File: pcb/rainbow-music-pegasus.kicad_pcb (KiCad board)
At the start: 2 copper layers, 151 x 31 mm, 114 parts, among them J1 USB_B_Micro, J2 Conn_02x03_Odd_Even, J3 B2B-PH-K-S, Q1 DMG3415U, SW1 SW_SPDT, SW2 EVQQ2, U1 ESP32-C3-MINI-1, U2 OPA2322, U3 TLV75533PDBV, U4 MCP73831-2-OT, U5 MCP41050

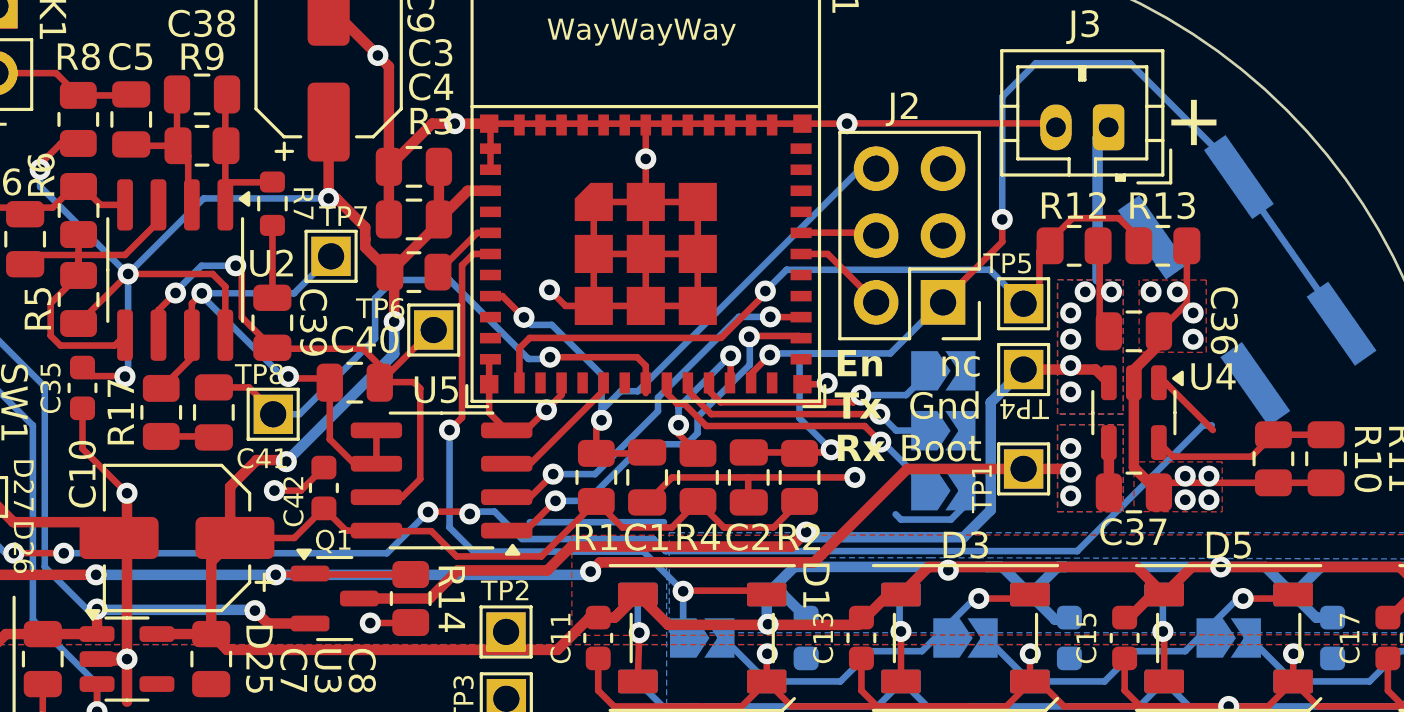
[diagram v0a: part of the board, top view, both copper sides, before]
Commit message: Minor changes to the PCB and BOM to better support the digipot and signal
* Remove C40 (which was shunting the MCP41050 PB0 & PB0, reducing effectiveness)
* Raise R7 from 470 to 2.2k
* Raise R17 from 100 to 330
* Change C41 to a 0.1uF shunt cap to GND placed close to GPIO4

The R7 is raised 2.2k so the digipot wiper current stays within its +/-1
mA rating even if the first stage swings rail to rail, and so loud music
sits mid-range on the wiper where steps are finer (maximum stage-2 gain
is now ~23). With C39 (2.2uF) this also lowers the high-pass corner from
~154 Hz to ~33 Hz, letting bass through.

The ADC now sees U2B's 1.65 V output directly, as the firmware expects,
and R17/C41 form a ~4.8 kHz anti-aliasing filter and a charge reservoir
for ADC sampling.
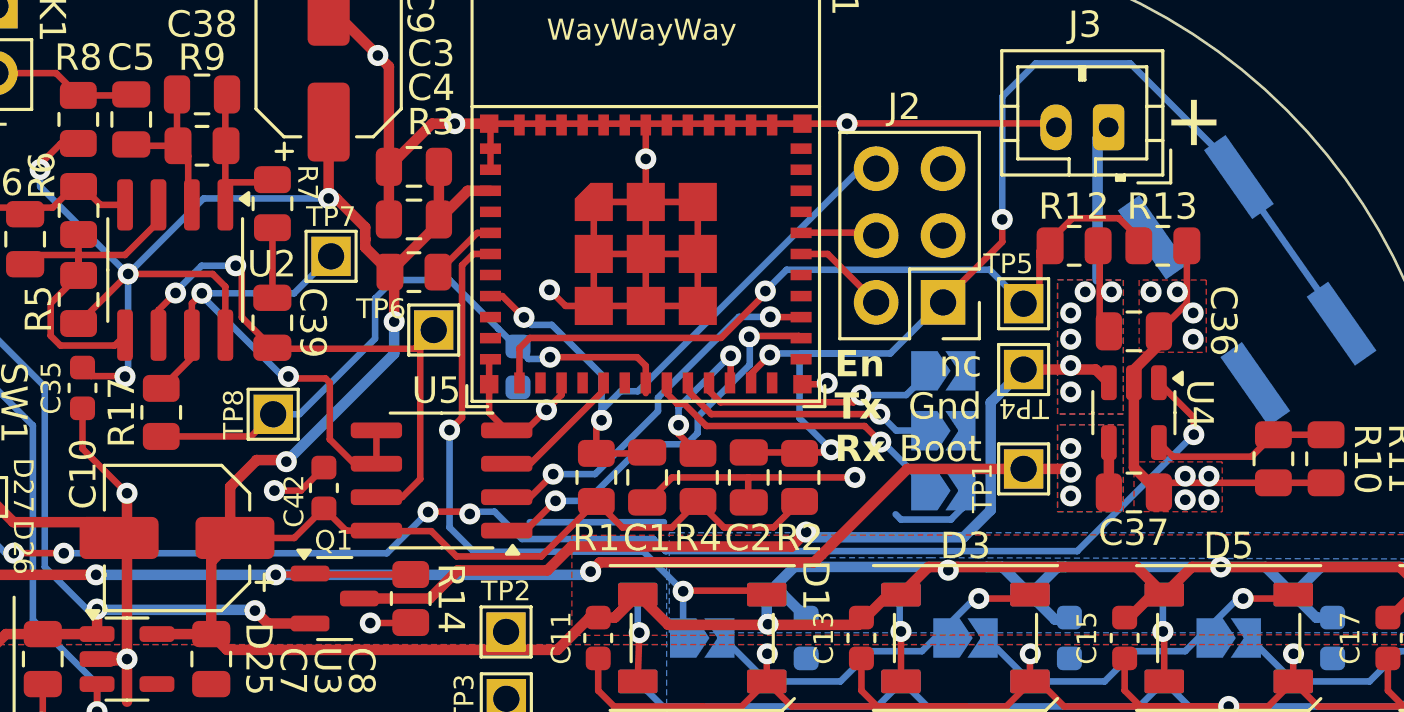
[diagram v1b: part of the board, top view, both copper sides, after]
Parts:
- removed C40: 4.7uF, Capacitor_SMD:C_0805_2012Metric
- C41: value 2.2uF -> 0.1uF; footprint Capacitor_SMD:C_0805_2012Metric -> Capacitor_SMD:C_0603_1608Metric; moved to B.Cu
- R17: value 100 -> 330
- R7: value 470 -> 2.2k; footprint Resistor_SMD:R_0603_1608Metric -> Resistor_SMD:R_0805_2012Metric
- moved C41 11.7 mm to (108.8, 90.3)
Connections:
- C41 pad 2: Net-(C41-Pad2) -> GND
- R17 pad 2: Net-(C41-Pad2) -> /Mic_Signal
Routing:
- net Net-(C41-Pad2): track 2.02 -> 0.00 mm
- net /Mic_Signal: track 22.4 -> 24.3 mm
- net Net-(U4-STAT): track 54.4 -> 53.3 mm, vias 4 -> 5
- net /DP_B: track 23.2 -> 22.6 mm
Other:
- board text added: "v1.1.1"
- board text removed: "v1.1"

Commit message: Move the button from GPIO9 to GPIO1
Eventually the button will be used as a factory reset (remove settings
like wifi configuration, etc) by holding down on power-on.  You cannot
do that with GPIO9 as that is already used to launch the bootloader on
power-on.

Actual button code and functionality still TBD.
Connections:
- C2 pad 2: /Boot -> /Button
- R2 pad 2: /Boot -> /Button
- SW2 pad 1: /Boot -> /Button
- U1 pad 13: unconnected-(U1-GPIO1/ADC1_CH1/XTAL_32K_N-Pad13) -> /Button
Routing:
- net /Button: track 0.00 -> 53.6 mm, vias 0 -> 3
- net /Boot: track 46.1 -> 11.8 mm, vias 3 -> 1
- net GND: track 458.8 -> 461.7 mm

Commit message: Change C38 to a 1.5nF C0G
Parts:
- C38: value 100pF -> 1.5nF C0G
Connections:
- C38 pad 1: Net-(U2A--) -> Net-(C38-Pad1)
- C38 pad 2: Net-(C38-Pad2) -> Net-(U2A--)
- R7 pad 1: Net-(C38-Pad2) -> Net-(C38-Pad1)
- R9 pad 1: Net-(C38-Pad2) -> Net-(U2A--)
- R9 pad 2: Net-(U2A--) -> Net-(C38-Pad1)
- U2 pad 1: Net-(C38-Pad2) -> Net-(C38-Pad1)
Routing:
- net Net-(U2A--): track 6.23 -> 13.0 mm
- net Net-(C38-Pad2): track 6.76 -> 0.00 mm
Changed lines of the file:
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@@
 			(layers "F.Cu" "F.Mask" "F.Paste")
 			(roundrect_rratio 0.243902)
-			(net "Net-(C38-Pad2)")
+			(net "Net-(C38-Pad1)")
 			(pintype "passive")
 		)
@@
 			)
 		)
-		(property "Value" "100pF"
+		(property "Value" "1.5nF C0G"
 			(at 0 1.68 0)
 			(layer "F.Fab")
@@
 			(layers "F.Cu" "F.Mask" "F.Paste")
 			(roundrect_rratio 0.25)
-			(net "Net-(U2A--)")
+			(net "Net-(C38-Pad1)")
 			(pintype "passive")
 		)
@@
 			(layers "F.Cu" "F.Mask" "F.Paste")
 			(roundrect_rratio 0.25)
-			(net "Net-(C38-Pad2)")
+			(net "Net-(U2A--)")
 			(pintype "passive")
 		)
@@
 			(layers "F.Cu" "F.Mask" "F.Paste")
 			(roundrect_rratio 0.25)
-			(net "Net-(C38-Pad2)")
+			(net "Net-(C38-Pad1)")
 			(pintype "output")
 		)
@@
 			(layers "F.Cu" "F.Mask" "F.Paste")
 			(roundrect_rratio 0.243902)
-			(net "Net-(C38-Pad2)")
+			(net "Net-(U2A--)")
 			(pintype "passive")
 		)
@@
 			(layers "F.Cu" "F.Mask" "F.Paste")
 			(roundrect_rratio 0.243902)
-			(net "Net-(U2A--)")
+			(net "Net-(C38-Pad1)")
 			(pintype "passive")
 		)
@@
 	)
 	(segment
-		(start 97.6825 84.145)
-		(end 97.6825 83.475)
+		(start 99.4725 87.67)
+		(end 99.4675 87.675)
 		(width 0.25)
 		(layer "F.Cu")
-		(net "Net-(C38-Pad2)")
+		(net "Net-(C39-Pad1)")
 	)
 	(segment
-		(start 97.6825 83.475)
-		(end 97.8675 83.29)
+		(start 99.4725 85.0125)
+		(end 99.4725 87.67)
 		(width 0.25)
 		(layer "F.Cu")
-		(net "Net-(C38-Pad2)")
+		(net "Net-(C39-Pad1)")
 	)
 	(segment
-		(start 99.4575 83.29)
-		(end 99.4725 83.275)
+		(start 97.6825 84.145)
+		(end 97.6825 83.475)
 		(width 0.25)
 		(layer "F.Cu")
-		(net "Net-(C38-Pad2)")
+		(net "Net-(U2A--)")
 	)
 	(segment
-		(start 97.8675 83.29)
-		(end 99.4575 83.29)
+		(start 97.6825 83.475)
+		(end 97.8675 83.29)
 		(width 0.25)
 		(layer "F.Cu")
-		(net "Net-(C38-Pad2)")
+		(net "Net-(U2A--)")
 	)
 	(segment
-		(start 97.6825 80.015)
-		(end 97.7475 79.95)
+		(start 94.1075 81.85)
+		(end 94.1575 81.9)
 		(width 0.25)
 		(layer "F.Cu")
-		(net "Net-(C38-Pad2)")
+		(net "Net-(U2A--)")
 	)
 	(segment
-		(start 97.6825 84.145)
-		(end 97.6825 80.015)
+		(start 96.2725 84.005)
+		(end 96.4125 84.145)
 		(width 0.25)
 		(layer "F.Cu")
-		(net "Net-(C38-Pad2)")
+		(net "Net-(U2A--)")
 	)
 	(segment
-		(start 99.4725 87.67)
-		(end 99.4675 87.675)
+		(start 94.1575 81.9)
+		(end 95.885 81.9)
 		(width 0.25)
 		(layer "F.Cu")
-		(net "Net-(C39-Pad1)")
+		(net "Net-(U2A--)")
 	)
 	(segment
-		(start 99.4725 85.0125)
-		(end 99.4725 87.67)
+		(start 95.8475 81.8625)
+		(end 95.885 81.9)
 		(width 0.25)
 		(layer "F.Cu")
-		(net "Net-(C39-Pad1)")
+		(net "Net-(U2A--)")
 	)
 	(segment
-		(start 94.1075 81.85)
-		(end 94.1575 81.9)
+		(start 99.4575 83.29)
+		(end 99.4725 83.275)
 		(width 0.25)
 		(layer "F.Cu")
@@
 	)
 	(segment
-		(start 96.2725 84.005)
-		(end 96.4125 84.145)
+		(start 95.885 81.9)
+		(end 96.2725 82.2875)
 		(width 0.25)
 		(layer "F.Cu")
@@
 	)
 	(segment
-		(start 94.1575 81.9)
-		(end 95.885 81.9)
+		(start 96.2725 82.2875)
+		(end 96.2725 84.005)
 		(width 0.25)
 		(layer "F.Cu")
@@
 	)
 	(segment
-		(start 95.8475 81.8625)
-		(end 95.885 81.9)
+		(start 97.8675 83.29)
+		(end 99.4575 83.29)
 		(width 0.25)
 		(layer "F.Cu")
@@
 	)
 	(segment
-		(start 95.885 81.9)
-		(end 96.2725 82.2875)
+		(start 97.6825 80.015)
+		(end 97.7475 79.95)
 		(width 0.25)
 		(layer "F.Cu")
@@
 	)
 	(segment
-		(start 96.2725 82.2875)
-		(end 96.2725 84.005)
+		(start 95.8475 79.95)
+		(end 95.8475 81.8625)
 		(width 0.25)
 		(layer "F.Cu")
@@
 	)
 	(segment
-		(start 95.8475 79.95)
-		(end 95.8475 81.8625)
+		(start 97.6825 84.145)
+		(end 97.6825 80.015)
 		(width 0.25)
 		(layer "F.Cu")

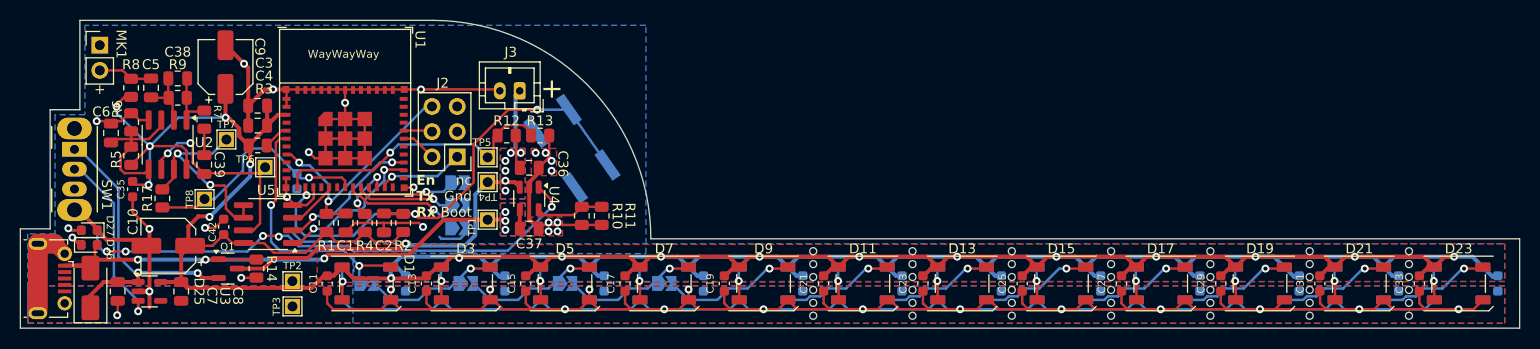
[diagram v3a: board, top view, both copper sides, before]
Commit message: Run DRC, adjust some cap placements
Cleaned up errors.  Still lots of warnings re: silkscreen violations
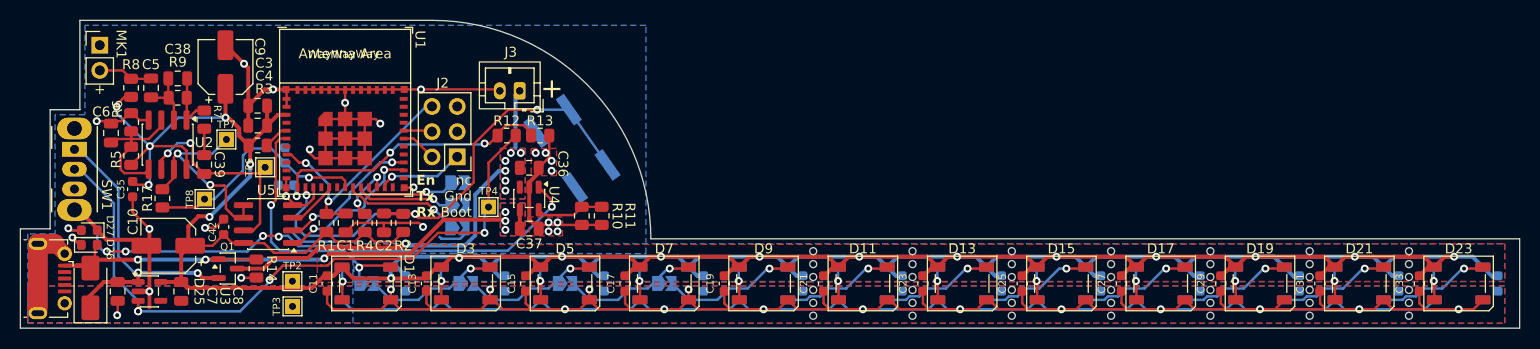
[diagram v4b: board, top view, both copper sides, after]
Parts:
- removed TP1, TP5: TestPoint, TestPoint:TestPoint_THTPad_1.5x1.5mm_Drill0.7mm
- added C40: 0.1uF, Capacitor_SMD:C_0603_1608Metric, B.Cu at (107.7, 90.7)
- moved C41 2.86 mm to (107.6, 87.7), turned to 90 degrees
- moved TP4 2.50 mm to (128.1, 92.9)
- turned C38 to 180 degrees
- turned R9 to 0 degrees
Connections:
- R12 pad 2: +BATT -> /SW_COM
- SW1 pad 2: Net-(SW1-B) -> /SW_COM
- TP4 pad 1: +BATT -> /SW_COM
- U3 pad 3: Net-(SW1-B) -> /SW_COM
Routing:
- net /SW_COM: track 0.00 -> 68.4 mm, vias 0 -> 4
- net Net-(SW1-B): track 18.3 -> 0.00 mm, vias 1 -> 0
- net Net-(C38-Pad1): track 0.00 -> 7.00 mm
- net Net-(U2A--): track 13.0 -> 6.43 mm
- net +BATT: track 44.2 -> 39.6 mm
- net GND: track 461.7 -> 463.7 mm, vias 36 -> 37
- net /Batt_Level: track 28.8 -> 30.2 mm, vias 1 -> 3

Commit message: Final cleanup of all DRC warnings — added to TODO to upgrade to USB-C
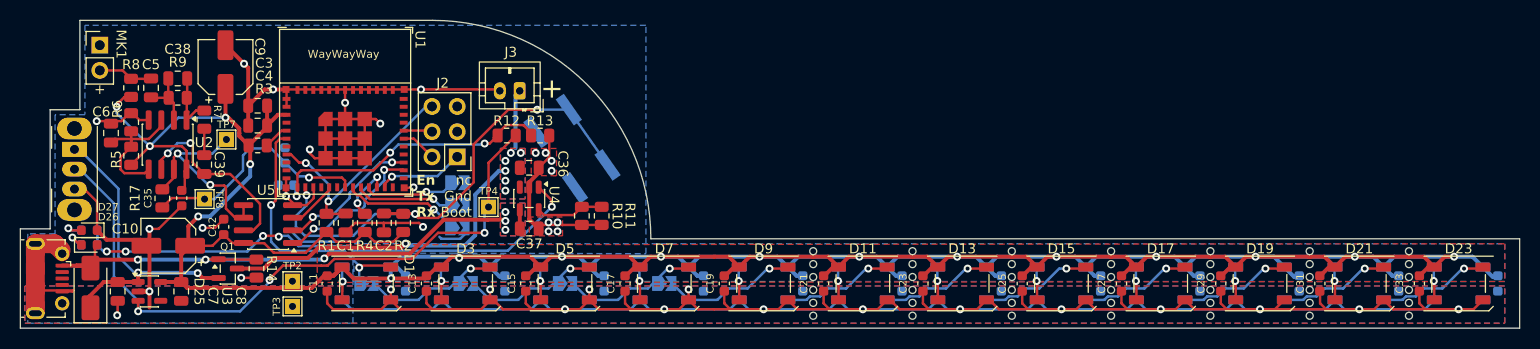
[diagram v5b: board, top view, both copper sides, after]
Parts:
- removed TP6: TestPoint, TestPoint:TestPoint_THTPad_1.5x1.5mm_Drill0.7mm
- SW1: footprint Button_Switch_THT:SW_CuK_OS102011MA1QN1_SPDT_Angled -> Button_Switch_THT:SW_Slide_SPDT_Angled_CK_OS102011MA1Q
- moved C35 5.02 mm to (97.2, 92.0)
- moved J1 0.25 mm to (83.7, 100.1)
- turned TP8 to 180 degrees
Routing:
- net GND: track 463.7 -> 471.6 mm
- net +3.3V: track 397.1 -> 393.6 mm, vias 18 -> 17
- net /DP_B: track 22.6 -> 19.2 mm
- net /SW_COM: vias 4 -> 3

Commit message: Replaced the dual 0603 power status LEDs with a LTST-C195KGJRKT
A little easier to place as the orientation is clear.
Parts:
- removed D27: GREEN, LED_SMD:LED_0603_1608Metric
- removed TP7: TestPoint, TestPoint:TestPoint_THTPad_1.5x1.5mm_Drill0.7mm
- C38: value 1.5nF C0G -> 6.8nF C0G
- D26: value RED -> LTST-C195KGJRKT; footprint LED_SMD:LED_0603_1608Metric -> Altivo:LTST-C195KGJRKT
- MK1: value Microphone -> AOM-5024P-HD-MB-R
- R9: value 10k -> 2.2k
- moved TP1 1.30 mm to (100.8, 92.1), turned to 0 degrees
- moved D26 0.73 mm to (87.7, 96.0), turned to 180 degrees
- moved C6 0.65 mm to (90.1, 86.1)
- moved G*** 0.36 mm to (97.0, 92.2)
- renumbered TP8 to TP1
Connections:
- D26 pad 1: Net-(D26-K) -> Net-(D26-A2)
- R15 pad 2: Net-(D26-K) -> Net-(D26-K1)
- R16 pad 1: Net-(D27-A) -> Net-(D26-A2)
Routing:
- net GND: track 471.6 -> 463.4 mm
- net /DP_W: track 22.0 -> 16.5 mm
- net Net-(D26-A2): track 0.00 -> 5.32 mm, vias 0 -> 1
- net Net-(D27-A): track 2.78 -> 0.00 mm, vias 1 -> 0
- net VBUS: track 58.5 -> 61.3 mm
- net /Mic_Signal: track 23.9 -> 21.3 mm, vias 1 -> 2
- net Net-(D26-K1): track 0.00 -> 2.39 mm, vias 0 -> 1
- net Net-(D26-K): track 2.08 -> 0.00 mm, vias 1 -> 0
- net +3.3V: track 393.6 -> 394.6 mm
